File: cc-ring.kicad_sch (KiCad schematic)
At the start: 39 parts, among them J1 Battery, J2 Charge/debug, J3 Battery, U1 STM32L431CCYx, U2 BQ297xy, U3 CSD83325L

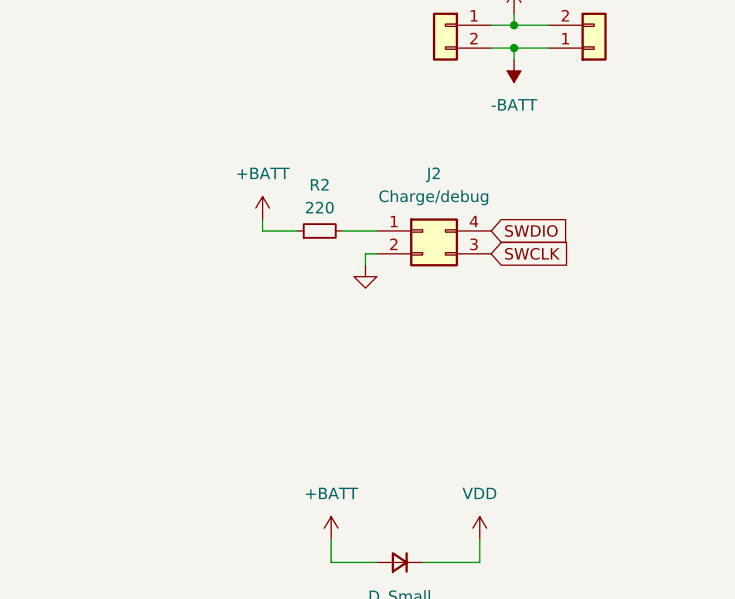
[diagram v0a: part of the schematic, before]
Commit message: magnetic charge connector
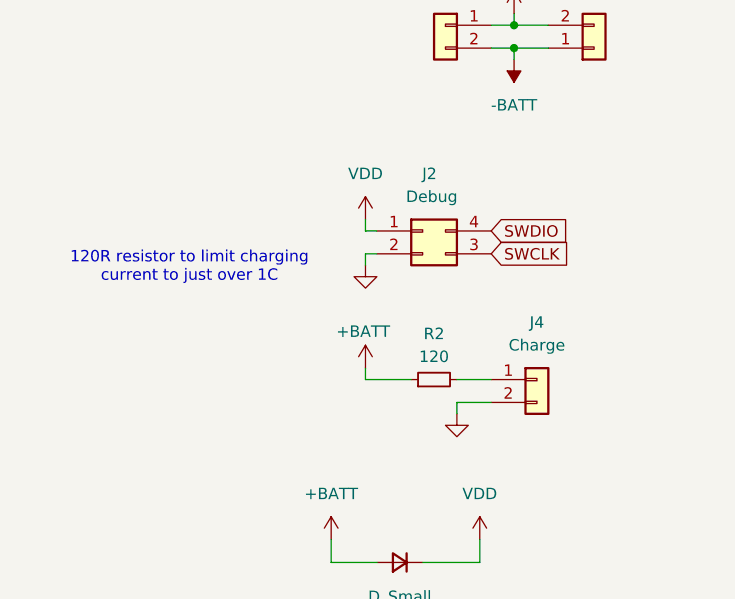
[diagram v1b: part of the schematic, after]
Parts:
- added J4: Charge, SolderPads:MageneticChargeConnector, symbol Connector_Generic:Conn_01x02
- J2: value Charge/debug -> Debug
- R2: value 220 -> 120
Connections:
- net GND: now also J4.2 (Pin_2)
- net VDD: now also J2.1 (Pin_1)
- net at R2.2: now also J4.1 (Pin_1); no longer J2.1 (Pin_1)
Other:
- note added: "120R resistor to limit charging current to just over 1C"

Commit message: update layout for magentic charge
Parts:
- D10: footprint Diode_SMD:D_0402_1005Metric -> Diode_SMD:D_SOD-523
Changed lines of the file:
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@@
 			)
 		)
-		(property "Footprint" "Diode_SMD:D_0402_1005Metric"
+		(property "Footprint" "Diode_SMD:D_SOD-523"
 			(at 52.07 88.9 90)
 			(effects

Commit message: make it manufacturable lol
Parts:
- removed D10: D_Small, Diode_SMD:D_SOD-523, symbol Device:D_Small
- removed R1: 1M, Resistor_SMD:R_0402_1005Metric, symbol Device:R_Small
- added C14, C15: 100n, Capacitor_SMD:C_0402_1005Metric, symbol Device:C_Small
- added U4: TLV70736DQNR, tlv707:DQN0004A, symbol tlv707:TLV70736DQNR
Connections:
- net +BATT: now also C15.1, U4.3 (EN), U4.4 (IN)
- net -BATT: no longer J1.2 (Pin_2), J3.1 (Pin_1), U3.C1 (S1)
- net GND: now also C14.2, C15.2, U4.2 (GND)
- net VDD: now also C14.1, U4.1 (OUT)
- new net -BATT2: J1.2 (Pin_2), J3.1 (Pin_1), U3.C1 (S1)
- no-connect marks 35 -> 36
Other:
- moved on the sheet: C2, C3, C4, C5, U1
